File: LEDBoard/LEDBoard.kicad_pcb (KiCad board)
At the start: 4 copper layers, 35 x 35 mm, 127 parts, among them J1 X0511FVS-24AS-LPV01, J2 X0511FVS-24AS-LPV01, Q1 AO3401A, SW1 SKRTLA

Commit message: Minor board updates
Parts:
- added C2: 1uF, Capacitor_SMD:C_0402_1005Metric, B.Cu at (103.5, 92.2)
- added C3: 10uF, Capacitor_SMD:C_0603_1608Metric, B.Cu at (104.5, 106.0)
- moved R5 19.1 mm to (123.5, 86.5)
- moved R6 17.0 mm to (126.0, 86.5), turned to 90 degrees
- moved Q1 1.00 mm to (104.0, 102.8)
- moved C1 0.25 mm to (101.8, 92.2)
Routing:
- net /LED2: track 31.0 -> 7.59 mm
- net /LED3_R: track 1.85 -> 22.2 mm
- net /LED3: track 26.0 -> 5.92 mm
- net /LED2_R: track 27.3 -> 37.3 mm
- net /LED Array/COL0: track 26.9 -> 27.4 mm
- net -BATT: track 10.1 -> 10.2 mm, vias 21 -> 23
- net +BATT: vias 8 -> 9

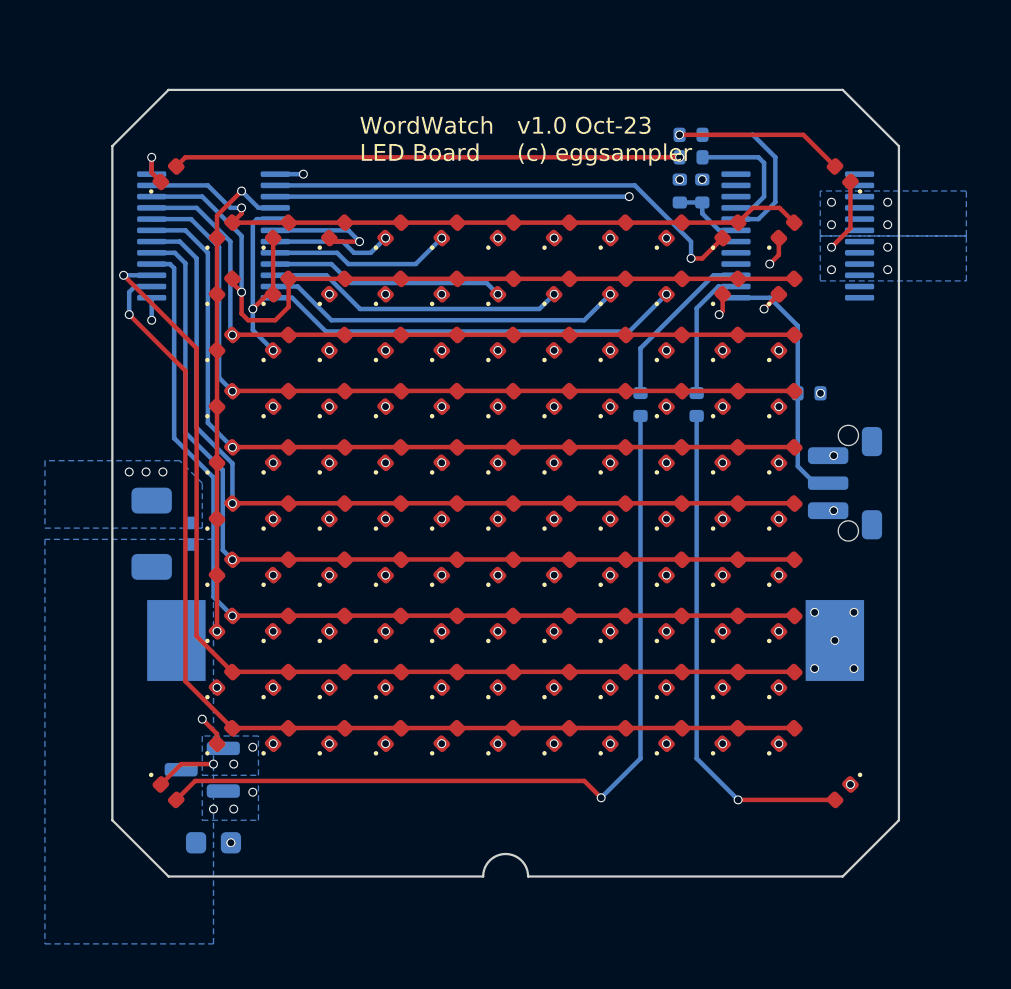
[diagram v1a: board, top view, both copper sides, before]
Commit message: Remove LED driver
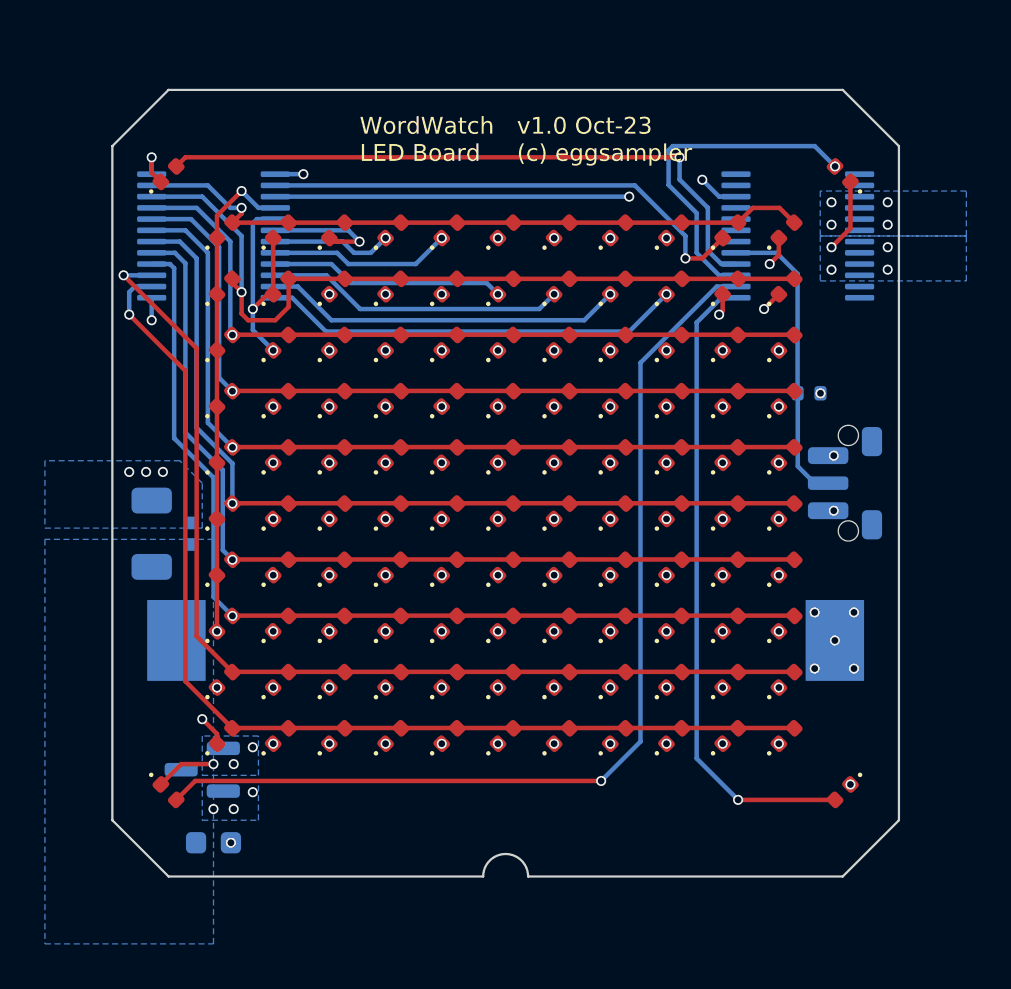
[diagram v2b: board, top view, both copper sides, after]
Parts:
- removed R1, R2: 1M, Resistor_SMD:R_0402_1005Metric
- removed R3, R4, R5, R6: 2.2k, Resistor_SMD:R_0402_1005Metric
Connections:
- D1 pad 2: /LED0_R -> /LED0
- D2 pad 2: /LED1_R -> /LED1
- D3 pad 2: /LED2_R -> /LED2
- D4 pad 2: /LED3_R -> /LED3
- J2 pad 1: unconnected-(J2-Pin_1-Pad1) -> +BATT
- J2 pad 10: /LED1 -> unconnected-(J2-Pin_10-Pad10)
- J2 pad 12: /VSENSE -> unconnected-(J2-Pin_12-Pad12)
- J2 pad 16: unconnected-(J2-Pin_16-Pad16) -> /BUTTON
- J2 pad 18: unconnected-(J2-Pin_18-Pad18) -> /LED0
- J2 pad 20: /LED2 -> /LED1
- J2 pad 21: unconnected-(J2-Pin_21-Pad21) -> -BATT
- J2 pad 22: /LED3 -> /LED2
- J2 pad 23: unconnected-(J2-Pin_23-Pad23) -> -BATT
- J2 pad 24: /BUTTON -> /LED3
- J2 pad 3: unconnected-(J2-Pin_3-Pad3) -> +BATT
- J2 pad 6: unconnected-(J2-Pin_6-Pad6) -> -BATT
- J2 pad 8: /LED0 -> unconnected-(J2-Pin_8-Pad8)
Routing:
- net /LED2_R: track 37.3 -> 0.00 mm, vias 1 -> 0
- net /LED2: track 7.59 -> 44.2 mm, vias 0 -> 1
- net /LED0: track 5.80 -> 28.7 mm, vias 0 -> 1
- net /LED3: track 5.92 -> 28.5 mm, vias 0 -> 1
- net /LED0_R: track 22.6 -> 0.00 mm, vias 1 -> 0
- net /LED3_R: track 22.2 -> 0.00 mm, vias 1 -> 0
- net /LED1_R: track 7.50 -> 0.00 mm, vias 1 -> 0
- net /LED1: track 7.71 -> 15.1 mm, vias 0 -> 1
- net /VSENSE: track 3.30 -> 0.00 mm
- net /BUTTON: track 11.2 -> 13.4 mm
- net -BATT: track 10.2 -> 12.0 mm
- net +BATT: vias 9 -> 8

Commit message: Small fixes for plotting
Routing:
- net /LED1: track 15.1 -> 13.5 mm
- net -BATT: vias 23 -> 25
- net +BATT: vias 8 -> 9

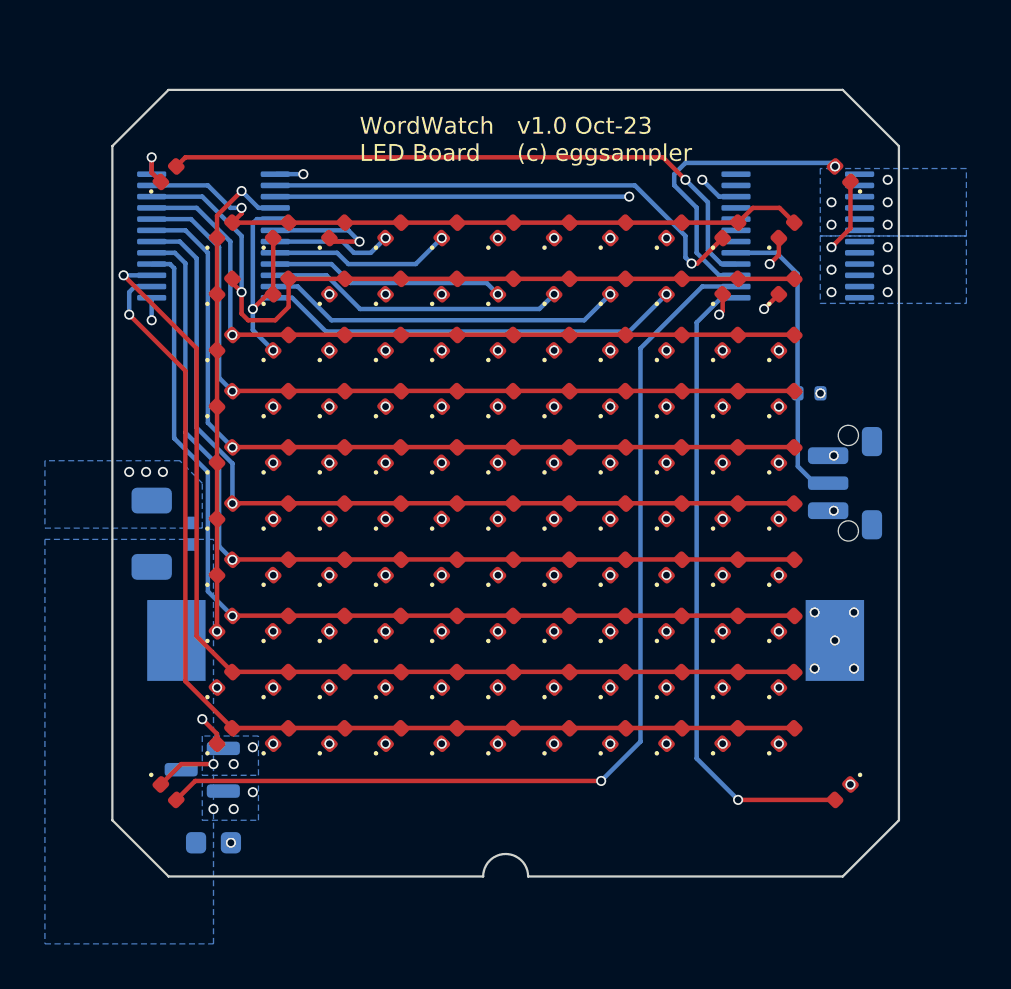
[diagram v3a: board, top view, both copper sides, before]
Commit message: Remove all via in pad on led board where possible
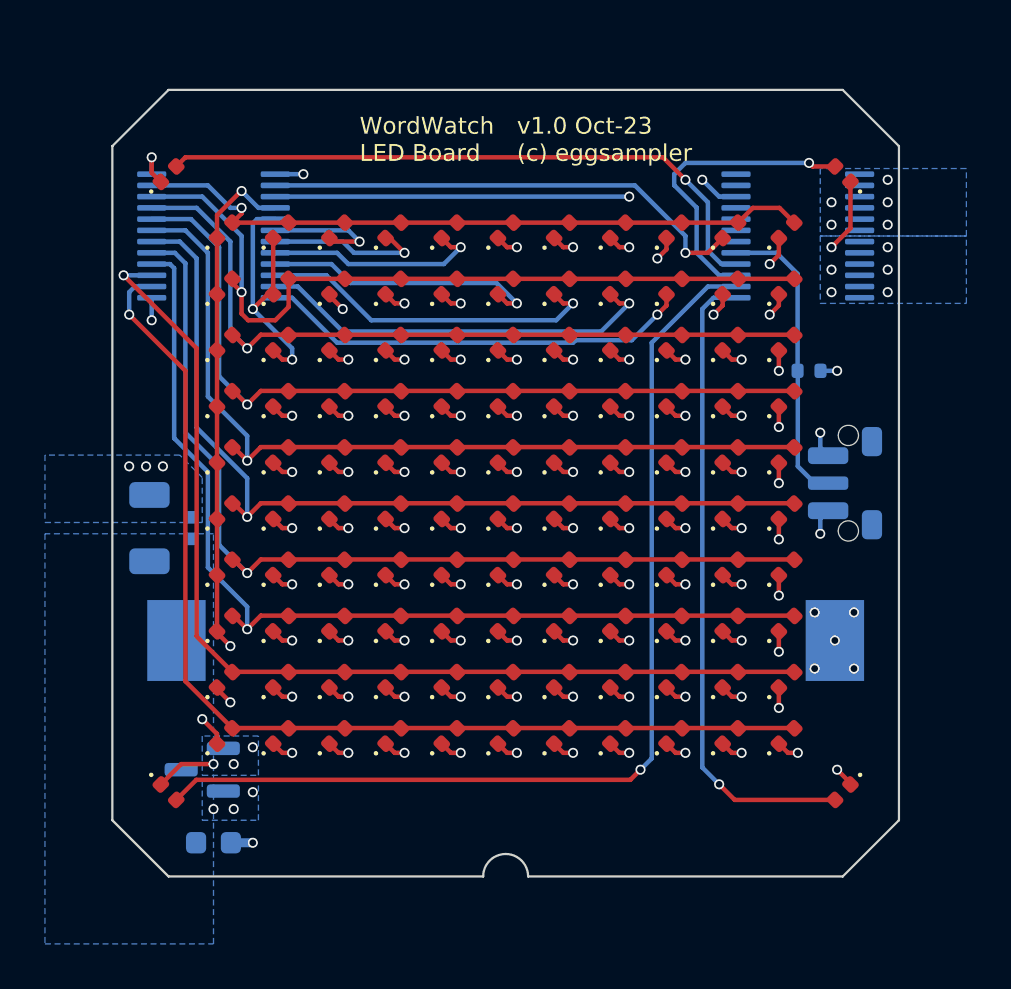
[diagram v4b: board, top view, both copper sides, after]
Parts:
- moved R7 1.00 mm to (131.0, 85.0)
- moved C1 0.27 mm to (101.7, 92.0)
- moved C2 0.25 mm to (103.5, 92.0)
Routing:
- net /LED Array/COL7: track 38.5 -> 49.7 mm
- net /LED Array/COL6: track 35.8 -> 47.0 mm
- net /LED Array/COL5: track 33.0 -> 44.1 mm
- net /LED Array/COL4: track 30.6 -> 41.4 mm
- net /LED Array/COL3: track 27.9 -> 38.4 mm
- net /LED Array/COL8: track 41.2 -> 51.1 mm
- net /LED Array/COL2: track 28.3 -> 37.5 mm
- net /LED Array/COL9: track 45.3 -> 54.3 mm
- net /LED Array/COL1: track 28.3 -> 37.1 mm
- net /LED Array/COL10: track 47.2 -> 55.3 mm
- net -BATT: track 12.0 -> 16.3 mm
- net /LED Array/COL0: track 27.4 -> 29.1 mm
- net /LED Array/ROW7: track 42.6 -> 44.0 mm
- net /LED Array/ROW6: track 40.8 -> 42.1 mm
- net /LED Array/ROW3: track 35.2 -> 36.5 mm
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
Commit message: Change led matrix routing for sinking current through mcu, sourcing from battery
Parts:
- added C4: 1uF, Capacitor_SMD:C_0402_1005Metric, B.Cu at (131.8, 86.6)
- added Q10: DMG1012T, Package_TO_SOT_SMD:SOT-523, B.Cu at (115.0, 84.5)
- added Q11: DMG1012T, Package_TO_SOT_SMD:SOT-523, B.Cu at (112.5, 84.5)
- added Q2: DMG1012T, Package_TO_SOT_SMD:SOT-523, B.Cu at (112.5, 74.5)
- added Q3: DMG1012T, Package_TO_SOT_SMD:SOT-523, B.Cu at (115.0, 74.5)
- added Q4: DMG1012T, Package_TO_SOT_SMD:SOT-523, B.Cu at (117.5, 74.5)
- added Q5: DMG1012T, Package_TO_SOT_SMD:SOT-523, B.Cu at (120.0, 74.5)
- added Q6: DMG1012T, Package_TO_SOT_SMD:SOT-523, B.Cu at (122.5, 74.5)
- added Q7: DMG1012T, Package_TO_SOT_SMD:SOT-523, B.Cu at (122.5, 84.5)
- added Q8: DMG1012T, Package_TO_SOT_SMD:SOT-523, B.Cu at (120.0, 84.5)
- added Q9: DMG1012T, Package_TO_SOT_SMD:SOT-523, B.Cu at (117.5, 84.5)
- added R13: 1k, Resistor_SMD:R_0402_1005Metric, B.Cu at (112.0, 76.8)
- added R14: 1k, Resistor_SMD:R_0402_1005Metric, B.Cu at (113.0, 76.8)
- added R15: 1k, Resistor_SMD:R_0402_1005Metric, B.Cu at (114.5, 76.8)
- added R16: 1k, Resistor_SMD:R_0402_1005Metric, B.Cu at (115.5, 76.8)
- added R17: 1k, Resistor_SMD:R_0402_1005Metric, B.Cu at (117.0, 76.8)
- added R18: 1k, Resistor_SMD:R_0402_1005Metric, B.Cu at (118.0, 76.8)
- added R19: 1k, Resistor_SMD:R_0402_1005Metric, B.Cu at (119.5, 76.8)
- added R20: 1k, Resistor_SMD:R_0402_1005Metric, B.Cu at (120.5, 76.8)
- added R21: 1k, Resistor_SMD:R_0402_1005Metric, B.Cu at (122.0, 76.8)
- added R22: 1k, Resistor_SMD:R_0402_1005Metric, B.Cu at (123.0, 76.8)
- added R23: 1k, Resistor_SMD:R_0402_1005Metric, B.Cu at (122.0, 82.2)
- added R24: 1k, Resistor_SMD:R_0402_1005Metric, B.Cu at (123.0, 82.2)
- added R25: 1k, Resistor_SMD:R_0402_1005Metric, B.Cu at (120.5, 82.2)
- added R26: 1k, Resistor_SMD:R_0402_1005Metric, B.Cu at (119.5, 82.2)
- added R27: 1k, Resistor_SMD:R_0402_1005Metric, B.Cu at (117.0, 82.2)
- added R28: 1k, Resistor_SMD:R_0402_1005Metric, B.Cu at (118.0, 82.2)
- added R29: 1k, Resistor_SMD:R_0402_1005Metric, B.Cu at (114.5, 82.2)
- added R30: 1k, Resistor_SMD:R_0402_1005Metric, B.Cu at (115.5, 82.2)
- added R31: 1k, Resistor_SMD:R_0402_1005Metric, B.Cu at (112.0, 82.2)
- added R32: 1k, Resistor_SMD:R_0402_1005Metric, B.Cu at (113.0, 82.2)
- R7: value 2.2k -> 10k
- moved R7 0.85 mm to (131.8, 85.4)
- moved J1 0.50 mm to (104.5, 79.5)
- moved J2 0.50 mm to (130.5, 79.5)
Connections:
- BT1 pad 2: -BATT -> GND
- C1 pad 2: -BATT -> GND
- C2 pad 2: -BATT -> GND
- C3 pad 2: -BATT -> GND
- D1 pad 1: -BATT -> GND
- D10 pad 2: /LED Array/ROW0 -> /LED Array/ROW0_S
- D100 pad 2: /LED Array/ROW8 -> /LED Array/ROW8_S
- D101 pad 2: /LED Array/ROW8 -> /LED Array/ROW8_S
- D102 pad 2: /LED Array/ROW8 -> /LED Array/ROW8_S
- D103 pad 2: /LED Array/ROW8 -> /LED Array/ROW8_S
- D104 pad 2: /LED Array/ROW9 -> /LED Array/ROW9_S
- D105 pad 2: /LED Array/ROW9 -> /LED Array/ROW9_S
- D106 pad 2: /LED Array/ROW9 -> /LED Array/ROW9_S
- D107 pad 2: /LED Array/ROW9 -> /LED Array/ROW9_S
- D108 pad 2: /LED Array/ROW9 -> /LED Array/ROW9_S
- D109 pad 2: /LED Array/ROW9 -> /LED Array/ROW9_S
- D11 pad 2: /LED Array/ROW0 -> /LED Array/ROW0_S
- D110 pad 2: /LED Array/ROW9 -> /LED Array/ROW9_S
- D111 pad 2: /LED Array/ROW9 -> /LED Array/ROW9_S
- D112 pad 2: /LED Array/ROW9 -> /LED Array/ROW9_S
- D113 pad 2: /LED Array/ROW9 -> /LED Array/ROW9_S
- D114 pad 2: /LED Array/ROW9 -> /LED Array/ROW9_S
- D12 pad 2: /LED Array/ROW0 -> /LED Array/ROW0_S
- D13 pad 2: /LED Array/ROW0 -> /LED Array/ROW0_S
- D14 pad 2: /LED Array/ROW0 -> /LED Array/ROW0_S
- D15 pad 2: /LED Array/ROW0 -> /LED Array/ROW0_S
- D16 pad 2: /LED Array/ROW1 -> /LED Array/ROW1_S
- D17 pad 2: /LED Array/ROW1 -> /LED Array/ROW1_S
- D18 pad 2: /LED Array/ROW1 -> /LED Array/ROW1_S
- D19 pad 2: /LED Array/ROW1 -> /LED Array/ROW1_S
- D2 pad 1: -BATT -> GND
- D20 pad 2: /LED Array/ROW1 -> /LED Array/ROW1_S
- D21 pad 2: /LED Array/ROW1 -> /LED Array/ROW1_S
- D22 pad 2: /LED Array/ROW1 -> /LED Array/ROW1_S
- D23 pad 2: /LED Array/ROW1 -> /LED Array/ROW1_S
- D24 pad 2: /LED Array/ROW1 -> /LED Array/ROW1_S
- D25 pad 2: /LED Array/ROW1 -> /LED Array/ROW1_S
- D26 pad 2: /LED Array/ROW1 -> /LED Array/ROW1_S
- D27 pad 2: /LED Array/ROW2 -> /LED Array/ROW2_S
- D28 pad 2: /LED Array/ROW2 -> /LED Array/ROW2_S
- D29 pad 2: /LED Array/ROW2 -> /LED Array/ROW2_S
- D3 pad 1: -BATT -> GND
- D30 pad 2: /LED Array/ROW2 -> /LED Array/ROW2_S
- D31 pad 2: /LED Array/ROW2 -> /LED Array/ROW2_S
- D32 pad 2: /LED Array/ROW2 -> /LED Array/ROW2_S
- D33 pad 2: /LED Array/ROW2 -> /LED Array/ROW2_S
- D34 pad 2: /LED Array/ROW2 -> /LED Array/ROW2_S
- D35 pad 2: /LED Array/ROW2 -> /LED Array/ROW2_S
- D36 pad 2: /LED Array/ROW2 -> /LED Array/ROW2_S
- D37 pad 2: /LED Array/ROW2 -> /LED Array/ROW2_S
- D38 pad 2: /LED Array/ROW3 -> /LED Array/ROW3_S
- D39 pad 2: /LED Array/ROW3 -> /LED Array/ROW3_S
- D4 pad 1: -BATT -> GND
- D40 pad 2: /LED Array/ROW3 -> /LED Array/ROW3_S
- D41 pad 2: /LED Array/ROW3 -> /LED Array/ROW3_S
- D42 pad 2: /LED Array/ROW3 -> /LED Array/ROW3_S
- D43 pad 2: /LED Array/ROW3 -> /LED Array/ROW3_S
- D44 pad 2: /LED Array/ROW3 -> /LED Array/ROW3_S
- D45 pad 2: /LED Array/ROW3 -> /LED Array/ROW3_S
- D46 pad 2: /LED Array/ROW3 -> /LED Array/ROW3_S
- D47 pad 2: /LED Array/ROW3 -> /LED Array/ROW3_S
- D48 pad 2: /LED Array/ROW3 -> /LED Array/ROW3_S
- D49 pad 2: /LED Array/ROW4 -> /LED Array/ROW4_S
- D5 pad 2: /LED Array/ROW0 -> /LED Array/ROW0_S
- D50 pad 2: /LED Array/ROW4 -> /LED Array/ROW4_S
- D51 pad 2: /LED Array/ROW4 -> /LED Array/ROW4_S
- D52 pad 2: /LED Array/ROW4 -> /LED Array/ROW4_S
- D53 pad 2: /LED Array/ROW4 -> /LED Array/ROW4_S
- D54 pad 2: /LED Array/ROW4 -> /LED Array/ROW4_S
- D55 pad 2: /LED Array/ROW4 -> /LED Array/ROW4_S
- D56 pad 2: /LED Array/ROW4 -> /LED Array/ROW4_S
- D57 pad 2: /LED Array/ROW4 -> /LED Array/ROW4_S
- D58 pad 2: /LED Array/ROW4 -> /LED Array/ROW4_S
- D59 pad 2: /LED Array/ROW4 -> /LED Array/ROW4_S
- D6 pad 2: /LED Array/ROW0 -> /LED Array/ROW0_S
- D60 pad 2: /LED Array/ROW5 -> /LED Array/ROW5_S
- D61 pad 2: /LED Array/ROW5 -> /LED Array/ROW5_S
- D62 pad 2: /LED Array/ROW5 -> /LED Array/ROW5_S
- D63 pad 2: /LED Array/ROW5 -> /LED Array/ROW5_S
- D64 pad 2: /LED Array/ROW5 -> /LED Array/ROW5_S
- D65 pad 2: /LED Array/ROW5 -> /LED Array/ROW5_S
- D66 pad 2: /LED Array/ROW5 -> /LED Array/ROW5_S
- D67 pad 2: /LED Array/ROW5 -> /LED Array/ROW5_S
- D68 pad 2: /LED Array/ROW5 -> /LED Array/ROW5_S
- D69 pad 2: /LED Array/ROW5 -> /LED Array/ROW5_S
- D7 pad 2: /LED Array/ROW0 -> /LED Array/ROW0_S
- D70 pad 2: /LED Array/ROW5 -> /LED Array/ROW5_S
- D71 pad 2: /LED Array/ROW6 -> /LED Array/ROW6_S
- D72 pad 2: /LED Array/ROW6 -> /LED Array/ROW6_S
- D73 pad 2: /LED Array/ROW6 -> /LED Array/ROW6_S
- D74 pad 2: /LED Array/ROW6 -> /LED Array/ROW6_S
- D75 pad 2: /LED Array/ROW6 -> /LED Array/ROW6_S
- D76 pad 2: /LED Array/ROW6 -> /LED Array/ROW6_S
- D77 pad 2: /LED Array/ROW6 -> /LED Array/ROW6_S
- D78 pad 2: /LED Array/ROW6 -> /LED Array/ROW6_S
- D79 pad 2: /LED Array/ROW6 -> /LED Array/ROW6_S
- D8 pad 2: /LED Array/ROW0 -> /LED Array/ROW0_S
- D80 pad 2: /LED Array/ROW6 -> /LED Array/ROW6_S
- D81 pad 2: /LED Array/ROW6 -> /LED Array/ROW6_S
- D82 pad 2: /LED Array/ROW7 -> /LED Array/ROW7_S
- D83 pad 2: /LED Array/ROW7 -> /LED Array/ROW7_S
- D84 pad 2: /LED Array/ROW7 -> /LED Array/ROW7_S
- D85 pad 2: /LED Array/ROW7 -> /LED Array/ROW7_S
- D86 pad 2: /LED Array/ROW7 -> /LED Array/ROW7_S
- D87 pad 2: /LED Array/ROW7 -> /LED Array/ROW7_S
- D88 pad 2: /LED Array/ROW7 -> /LED Array/ROW7_S
- D89 pad 2: /LED Array/ROW7 -> /LED Array/ROW7_S
- D9 pad 2: /LED Array/ROW0 -> /LED Array/ROW0_S
- D90 pad 2: /LED Array/ROW7 -> /LED Array/ROW7_S
- D91 pad 2: /LED Array/ROW7 -> /LED Array/ROW7_S
- D92 pad 2: /LED Array/ROW7 -> /LED Array/ROW7_S
- D93 pad 2: /LED Array/ROW8 -> /LED Array/ROW8_S
- D94 pad 2: /LED Array/ROW8 -> /LED Array/ROW8_S
- D95 pad 2: /LED Array/ROW8 -> /LED Array/ROW8_S
- D96 pad 2: /LED Array/ROW8 -> /LED Array/ROW8_S
- D97 pad 2: /LED Array/ROW8 -> /LED Array/ROW8_S
- D98 pad 2: /LED Array/ROW8 -> /LED Array/ROW8_S
- D99 pad 2: /LED Array/ROW8 -> /LED Array/ROW8_S
- J1 pad 1: -BATT -> GND
- J1 pad 10: /LED Array/ROW3 -> /LED Array/COL3
- J1 pad 11: /LED Array/COL2 -> /LED Array/ROW4
- J1 pad 12: /LED Array/ROW4 -> /LED Array/COL4
- J1 pad 13: /LED Array/COL3 -> /LED Array/ROW5
- J1 pad 14: /LED Array/ROW5 -> /LED Array/COL5
- J1 pad 15: /LED Array/COL4 -> /LED Array/ROW6
- J1 pad 16: /LED Array/ROW6 -> /LED Array/COL6
- J1 pad 17: /LED Array/COL5 -> /LED Array/ROW7
- J1 pad 18: /LED Array/ROW7 -> /LED Array/COL7
- J1 pad 19: /LED Array/COL6 -> /LED Array/ROW8
- J1 pad 2: -BATT -> GND
- J1 pad 20: /LED Array/ROW8 -> /LED Array/COL8
- J1 pad 21: /LED Array/COL7 -> /LED Array/ROW9
- J1 pad 22: /LED Array/ROW9 -> /LED Array/COL9
- J1 pad 23: /LED Array/COL8 -> GND
- J1 pad 24: -BATT -> /LED Array/COL10
- J1 pad 3: /LED Array/COL9 -> /LED Array/ROW0
- J1 pad 4: /LED Array/ROW0 -> /LED Array/COL0
- J1 pad 5: /LED Array/COL10 -> /LED Array/ROW1
- J1 pad 6: /LED Array/ROW1 -> /LED Array/COL1
- J1 pad 7: /LED Array/COL0 -> /LED Array/ROW2
- J1 pad 8: /LED Array/ROW2 -> /LED Array/COL2
- J1 pad 9: /LED Array/COL1 -> /LED Array/ROW3
- J2 pad 13: -BATT -> GND
- J2 pad 15: -BATT -> GND
- J2 pad 16: /BUTTON -> /LED0
- J2 pad 17: -BATT -> GND
- J2 pad 18: /LED0 -> /LED1
- J2 pad 19: -BATT -> GND
- J2 pad 20: /LED1 -> /LED2
- J2 pad 21: -BATT -> GND
- J2 pad 22: /LED2 -> /LED3
- J2 pad 23: -BATT -> GND
- J2 pad 24: /LED3 -> /BUTTON
- J2 pad 6: -BATT -> GND
- Q1 pad 1: -BATT -> GND
- SW1 pad 1: -BATT -> GND
- SW1 pad MP: (no net) -> GND
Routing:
- net /LED Array/ROW9_S: track 0.00 -> 51.7 mm, vias 0 -> 12
- net /LED Array/ROW4_S: track 0.00 -> 51.5 mm, vias 0 -> 12
- net /LED Array/ROW3_S: track 0.00 -> 51.2 mm, vias 0 -> 12
- net /LED Array/ROW8_S: track 0.00 -> 49.2 mm, vias 0 -> 12
- net /LED Array/ROW1_S: track 0.00 -> 48.1 mm, vias 0 -> 12
- net /LED Array/ROW2_S: track 0.00 -> 47.7 mm, vias 0 -> 12
- net /LED Array/ROW7_S: track 0.00 -> 46.7 mm, vias 0 -> 12
- net /LED Array/ROW6_S: track 0.00 -> 44.1 mm, vias 0 -> 12
- net /LED Array/ROW9: track 47.4 -> 4.75 mm, vias 1 -> 0
- net /LED Array/ROW5_S: track 0.00 -> 41.6 mm, vias 0 -> 12
- net /LED Array/ROW0_S: track 0.00 -> 41.6 mm, vias 0 -> 1
- net /LED Array/ROW8: track 45.9 -> 7.49 mm, vias 1 -> 0
- net /LED Array/ROW7: track 44.0 -> 10.2 mm, vias 1 -> 0
- net /LED Array/ROW6: track 42.1 -> 13.9 mm, vias 1 -> 0
- net /LED Array/ROW1: track 35.2 -> 7.49 mm, vias 1 -> 0
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- added copper zone on B.Cu, net GND
- added copper zone on F.Cu, net GND
- added copper zone on In1.Cu, net GND
- removed copper zone on B.Cu, net -BATT
- removed copper zone on In1.Cu, net -BATT
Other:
- board text added: "v1.0 Nov-23 (c) eggsampler"
- board text removed: "WordWatch LED Board v1.0 Oct-23 (c) eggsampler"
- board text removed: "v1.0 Oct-23 (c) eggsampler"
